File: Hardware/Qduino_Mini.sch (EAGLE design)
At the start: 41 parts, among them Q1 PFET, U1 ATMEGA32U41:1-LESS_PASTE, U2 MCP73831, U3 MAX17048, U4 TPS78233, U7 DNP, Y1 16MHZ

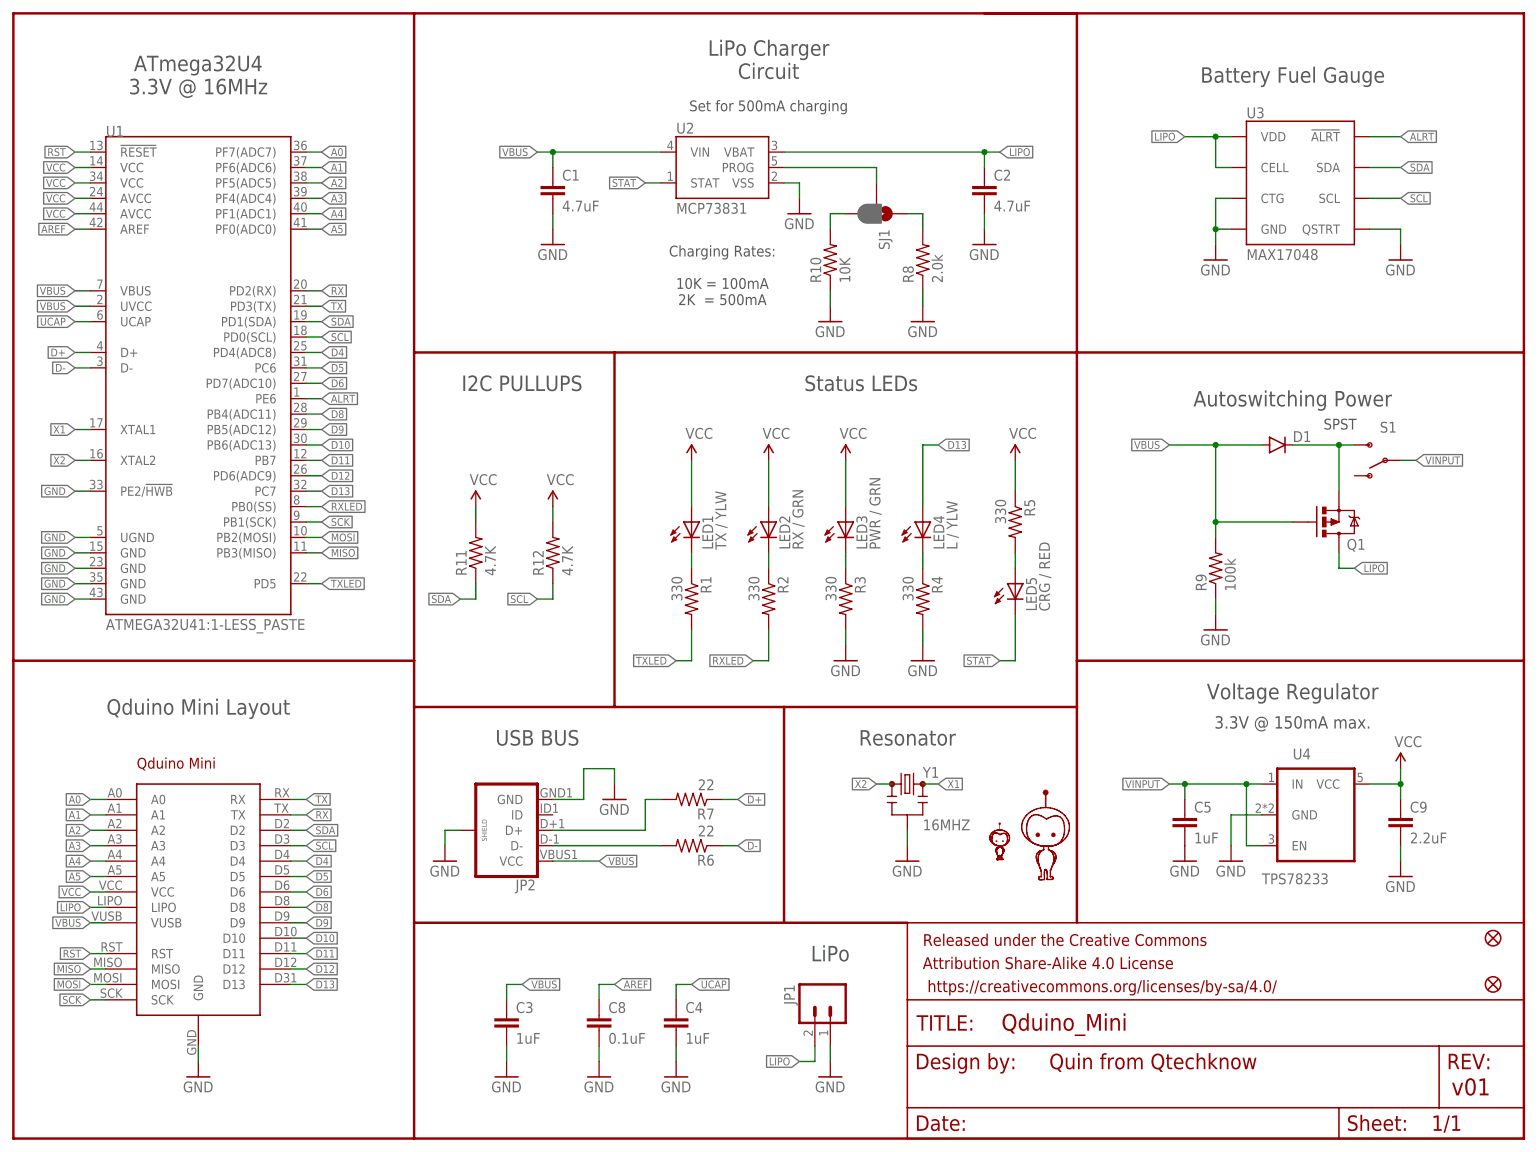
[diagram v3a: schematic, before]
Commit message: Dropped resonator to 8MHz for battery use & fixed some silk
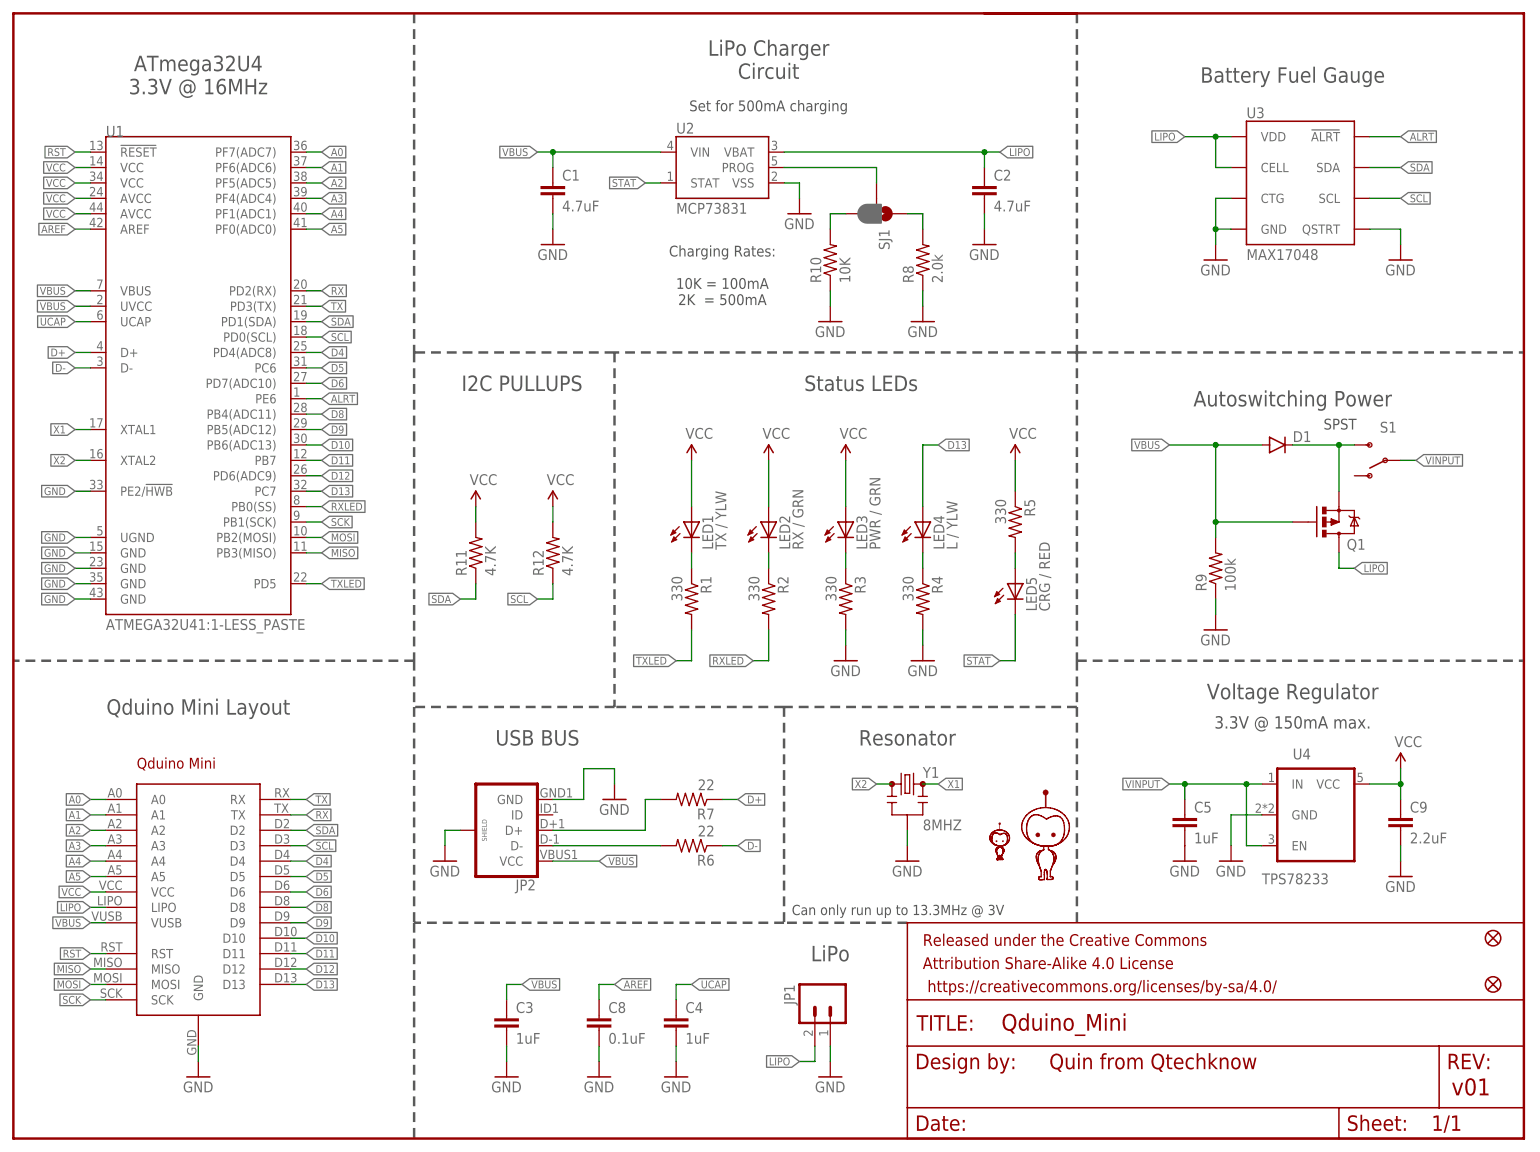
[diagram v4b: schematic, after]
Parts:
- U7: device Qtechknow:QDUINOMINI -> Qduino_Mini:QDUINOMINI
- Y1: value 16MHZ -> 8MHZ; device SparkFun-FreqCtrl:RESONATOR16MHZ -> SparkFun-FreqCtrl:RESONATOR8MHZ
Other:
- note added: "Can only run up to 13.3MHz @ 3V"
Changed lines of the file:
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@@
 <attribute name="PROD_ID" value="RES-07857"/>
 </part>
-<part name="U7" library="Qtechknow" deviceset="QDUINOMINI" device="" value="DNP"/>
+<part name="U7" library="Qduino_Mini" deviceset="QDUINOMINI" device="" value="DNP"/>
 <part name="P+2" library="SFE Aesthetics" deviceset="VCC" device=""/>
 <part name="R12" library="SparkFun-Passives" deviceset="RESISTOR" device="0603-RES" value="4.7K">
@@
 <part name="JP2" library="SparkFun-Connectors" deviceset="USB_MICROB_PLUG" device="CONN-11752"/>
 <part name="GND11" library="SFE Aesthetics" deviceset="GND" device=""/>
-<part name="Y1" library="SparkFun-FreqCtrl" deviceset="RESONATOR" device="16MHZ" value="16MHZ"/>
+<part name="Y1" library="SparkFun-FreqCtrl" deviceset="RESONATOR" device="8MHZ" value="8MHZ"/>
 <part name="GND22" library="SFE Aesthetics" deviceset="GND" device=""/>
 </parts>
@@
 <text x="-55.88" y="124.46" size="2.54" layer="97" align="center">ATmega32U4
 3.3V @ 16MHz</text>
-<wire x1="-20.32" y1="134.62" x2="-20.32" y2="78.74" width="0.4064" layer="94"/>
-<wire x1="-20.32" y1="78.74" x2="-20.32" y2="27.94" width="0.4064" layer="94"/>
-<wire x1="-20.32" y1="27.94" x2="-86.36" y2="27.94" width="0.4064" layer="94"/>
-<wire x1="-20.32" y1="27.94" x2="-20.32" y2="20.32" width="0.4064" layer="94"/>
+<wire x1="-20.32" y1="134.62" x2="-20.32" y2="78.74" width="0.4064" layer="97" style="shortdash"/>
+<wire x1="-20.32" y1="78.74" x2="-20.32" y2="27.94" width="0.4064" layer="97" style="shortdash"/>
+<wire x1="-20.32" y1="27.94" x2="-86.36" y2="27.94" width="0.4064" layer="97" style="shortdash"/>
+<wire x1="-20.32" y1="27.94" x2="-20.32" y2="20.32" width="0.4064" layer="97" style="shortdash"/>
 <text x="-55.88" y="20.32" size="2.54" layer="97" align="center">Qduino Mini Layout</text>
 <text x="38.1" y="127" size="2.54" layer="97" align="center">LiPo Charger
 Circuit</text>
-<wire x1="-20.32" y1="20.32" x2="-20.32" y2="-15.24" width="0.4064" layer="94"/>
-<wire x1="-20.32" y1="-15.24" x2="-20.32" y2="-50.8" width="0.4064" layer="94"/>
+<wire x1="-20.32" y1="20.32" x2="-20.32" y2="-15.24" width="0.4064" layer="97" style="shortdash"/>
+<wire x1="-20.32" y1="-15.24" x2="-20.32" y2="-50.8" width="0.4064" layer="97" style="shortdash"/>
 <wire x1="73.66" y1="134.62" x2="88.9" y2="134.62" width="0.4064" layer="94"/>
-<wire x1="88.9" y1="134.62" x2="88.9" y2="78.74" width="0.4064" layer="94"/>
-<wire x1="88.9" y1="78.74" x2="12.7" y2="78.74" width="0.4064" layer="94"/>
-<wire x1="12.7" y1="78.74" x2="-20.32" y2="78.74" width="0.4064" layer="94"/>
-<wire x1="88.9" y1="78.74" x2="88.9" y2="27.94" width="0.4064" layer="94"/>
-<wire x1="88.9" y1="27.94" x2="88.9" y2="20.32" width="0.4064" layer="94"/>
-<wire x1="88.9" y1="20.32" x2="40.64" y2="20.32" width="0.4064" layer="94"/>
-<wire x1="40.64" y1="20.32" x2="12.7" y2="20.32" width="0.4064" layer="94"/>
-<wire x1="12.7" y1="20.32" x2="-20.32" y2="20.32" width="0.4064" layer="94"/>
-<wire x1="88.9" y1="20.32" x2="88.9" y2="-15.24" width="0.4064" layer="94"/>
-<wire x1="60.96" y1="-15.24" x2="40.64" y2="-15.24" width="0.4064" layer="94"/>
-<wire x1="40.64" y1="-15.24" x2="-20.32" y2="-15.24" width="0.4064" layer="94"/>
-<wire x1="40.64" y1="20.32" x2="40.64" y2="-15.24" width="0.4064" layer="94"/>
+<wire x1="88.9" y1="134.62" x2="88.9" y2="78.74" width="0.4064" layer="97" style="shortdash"/>
+<wire x1="88.9" y1="78.74" x2="12.7" y2="78.74" width="0.4064" layer="97" style="shortdash"/>
+<wire x1="12.7" y1="78.74" x2="-20.32" y2="78.74" width="0.4064" layer="97" style="shortdash"/>
+<wire x1="88.9" y1="78.74" x2="88.9" y2="27.94" width="0.4064" layer="97" style="shortdash"/>
+<wire x1="88.9" y1="27.94" x2="88.9" y2="20.32" width="0.4064" layer="97" style="shortdash"/>
+<wire x1="88.9" y1="20.32" x2="40.64" y2="20.32" width="0.4064" layer="97" style="shortdash"/>
+<wire x1="40.64" y1="20.32" x2="12.7" y2="20.32" width="0.4064" layer="97" style="shortdash"/>
+<wire x1="12.7" y1="20.32" x2="-20.32" y2="20.32" width="0.4064" layer="97" style="shortdash"/>
+<wire x1="88.9" y1="20.32" x2="88.9" y2="-15.24" width="0.4064" layer="97" style="shortdash"/>
+<wire x1="60.96" y1="-15.24" x2="40.64" y2="-15.24" width="0.4064" layer="97" style="shortdash"/>
+<wire x1="40.64" y1="-15.24" x2="-20.32" y2="-15.24" width="0.4064" layer="97" style="shortdash"/>
+<wire x1="40.64" y1="20.32" x2="40.64" y2="-15.24" width="0.4064" layer="97" style="shortdash"/>
 <text x="124.46" y="124.46" size="2.54" layer="97" align="center">Battery Fuel Gauge</text>
 <text x="124.46" y="22.86" size="2.54" layer="97" align="center">Voltage Regulator</text>
-<wire x1="88.9" y1="27.94" x2="162.56" y2="27.94" width="0.4064" layer="94"/>
+<wire x1="88.9" y1="27.94" x2="162.56" y2="27.94" width="0.4064" layer="97" style="shortdash"/>
 <text x="124.46" y="71.12" size="2.54" layer="97" align="center">Autoswitching Power</text>
-<wire x1="88.9" y1="78.74" x2="162.56" y2="78.74" width="0.4064" layer="94"/>
+<wire x1="88.9" y1="78.74" x2="162.56" y2="78.74" width="0.4064" layer="97" style="shortdash"/>
 <text x="30.48" y="91.44" size="1.778" layer="97" align="center">Charging Rates:
 10K = 100mA
 2K  = 500mA</text>
 <text x="-2.54" y="73.66" size="2.54" layer="97" align="center">I2C PULLUPS</text>
-<wire x1="12.7" y1="78.74" x2="12.7" y2="20.32" width="0.4064" layer="94"/>
+<wire x1="12.7" y1="78.74" x2="12.7" y2="20.32" width="0.4064" layer="97" style="shortdash"/>
+<text x="41.91" y="-13.97" size="1.6764" layer="97">Can only run up to 13.3MHz @ 3V</text>
 </plain>
 <instances>

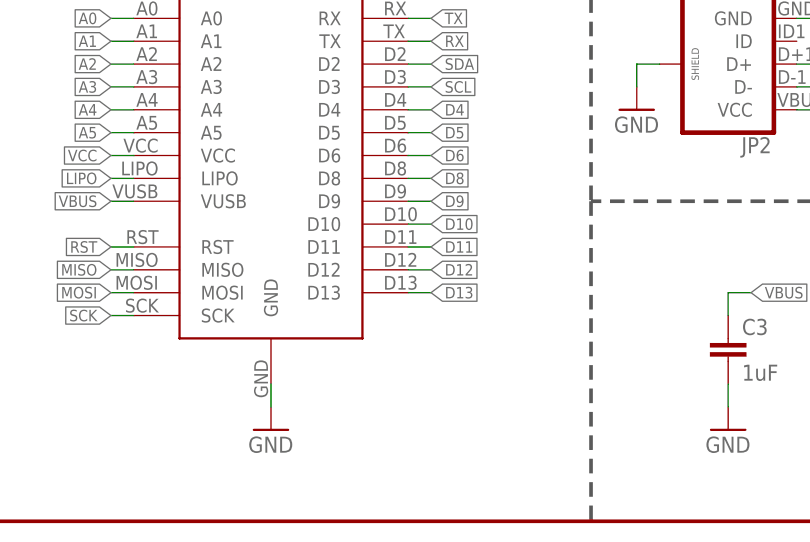
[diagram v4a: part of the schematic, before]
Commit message: Pushed silk around
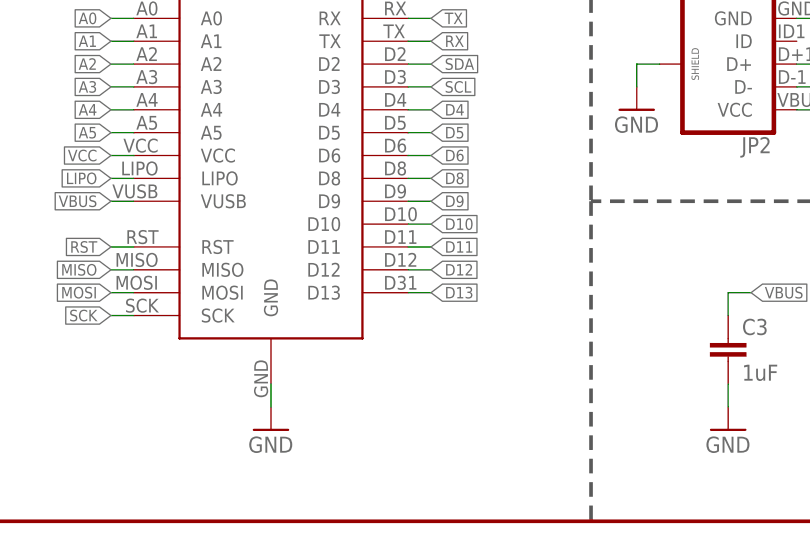
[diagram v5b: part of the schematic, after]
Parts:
- added U$7, U$8, U$9: QHEADERS, Qtechknow:QHEADERS
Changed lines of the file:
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@@
 <part name="Y1" library="SparkFun-FreqCtrl" deviceset="RESONATOR" device="8MHZ" value="8MHZ"/>
 <part name="GND22" library="SFE Aesthetics" deviceset="GND" device=""/>
+<part name="U$7" library="Qtechknow" deviceset="QHEADERS" device=""/>
+<part name="U$8" library="Qtechknow" deviceset="QHEADERS" device=""/>
+<part name="U$9" library="Qtechknow" deviceset="QHEADERS" device=""/>
 </parts>
 <sheets>
